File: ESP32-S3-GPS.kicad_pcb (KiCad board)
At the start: 2 copper layers, 75.6 x 87 mm, 46 parts, among them J1 PJ-102, J10 Conn_01x04_Pin, J11 Conn_01x04, J12 Conn_01x04, J2 Conn_01x03, J3 Conn_01x04, J4 Conn_01x05, J5 USB_B_Mini, J6 Conn_01x03_Pin, J7 Conn_01x02_Pin, J8 Conn_01x02_Pin, J9 Conn_02x04_Odd_Even, U1 AMS1117-5.0, U2 CH340N, U3 AMS1117-3.3, U5 ESP32-S3-DEVKITC-1-N8R2, U6 NRF24L01_Breakout

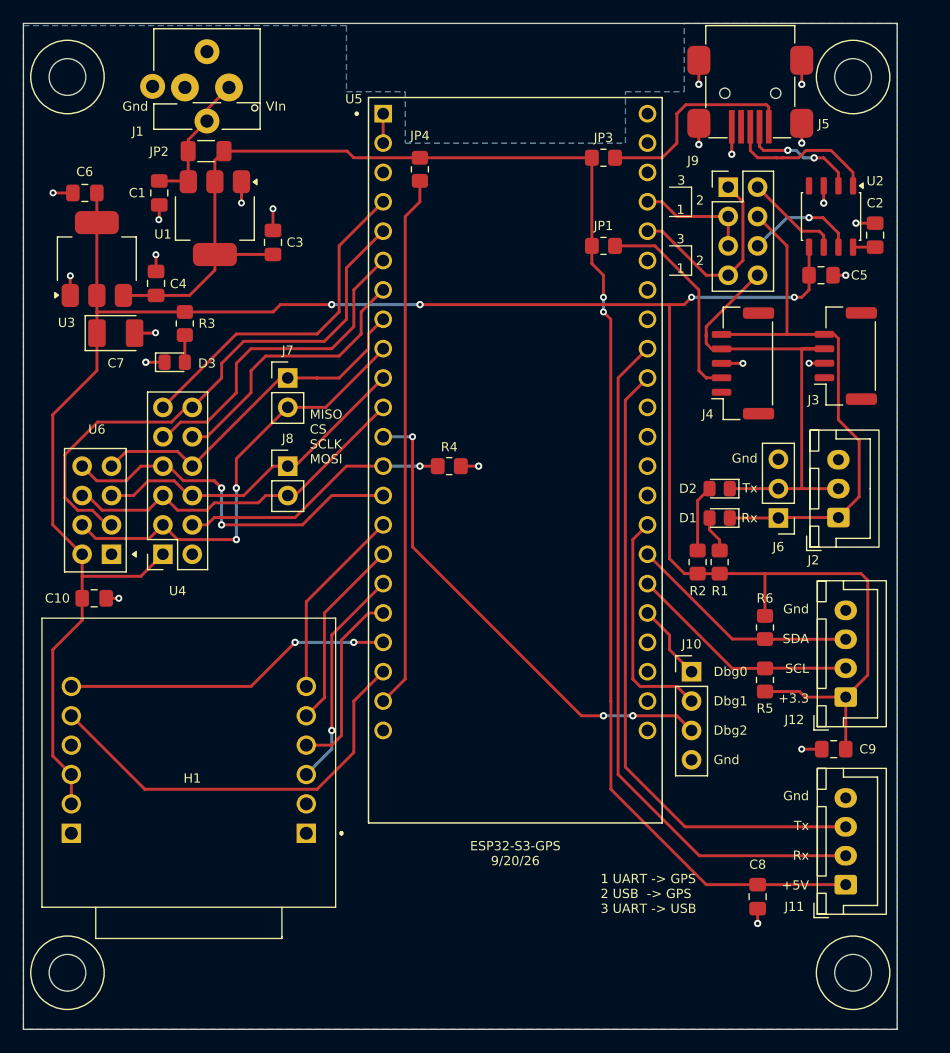
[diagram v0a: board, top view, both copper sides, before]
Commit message: Fix footprint for ESP32 DevKit Board.
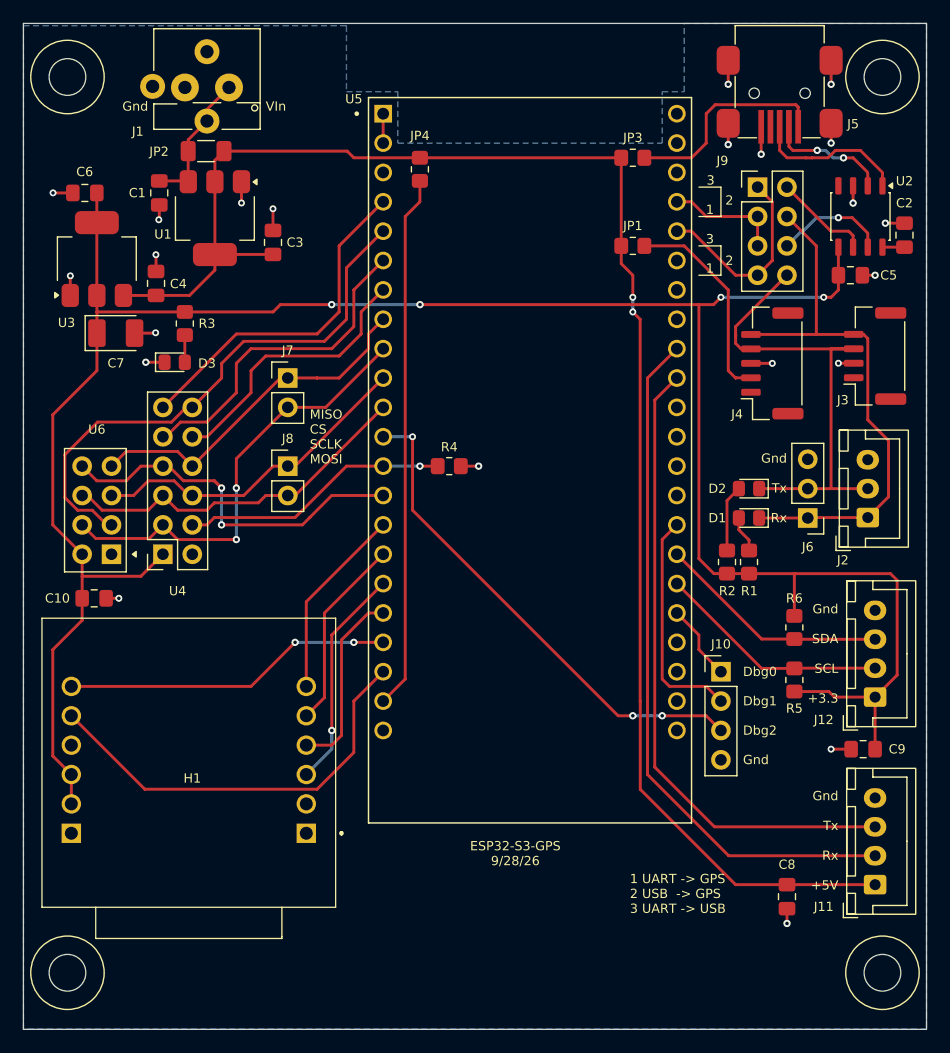
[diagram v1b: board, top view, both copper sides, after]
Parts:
- moved C5 2.54 mm to (188.4, 85.7)
- moved J2 2.54 mm to (189.9, 106.7)
- moved J4 2.54 mm to (181.6, 93.3)
- moved J6 2.54 mm to (184.7, 106.7)
- moved J9 2.54 mm to (180.3, 78.1)
- moved C2 2.54 mm to (193.0, 82.3)
- moved C8 2.54 mm to (182.9, 139.5)
- moved C9 2.54 mm to (189.5, 126.7)
- moved D1 2.54 mm to (179.6, 106.7)
- moved D2 2.54 mm to (179.6, 104.2)
- moved H4 2.54 mm to (191.1, 146.1)
- moved H5 2.54 mm to (191.1, 68.6)
- moved J10 2.54 mm to (177.2, 120.0)
- moved J11 2.54 mm to (190.5, 138.4)
- moved J12 2.54 mm to (190.5, 122.2)
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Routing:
- net +5V: track 135.5 -> 138.1 mm
- net +3V3: track 197.1 -> 199.6 mm
- net /Dbg2: track 42.8 -> 43.5 mm
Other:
- board size 75.6 x 87 mm -> 78.1 x 87 mm
- board text added: "ESP32-S3-GPS 9/28/26"
- board text removed: "ESP32-S3-GPS 9/20/26"

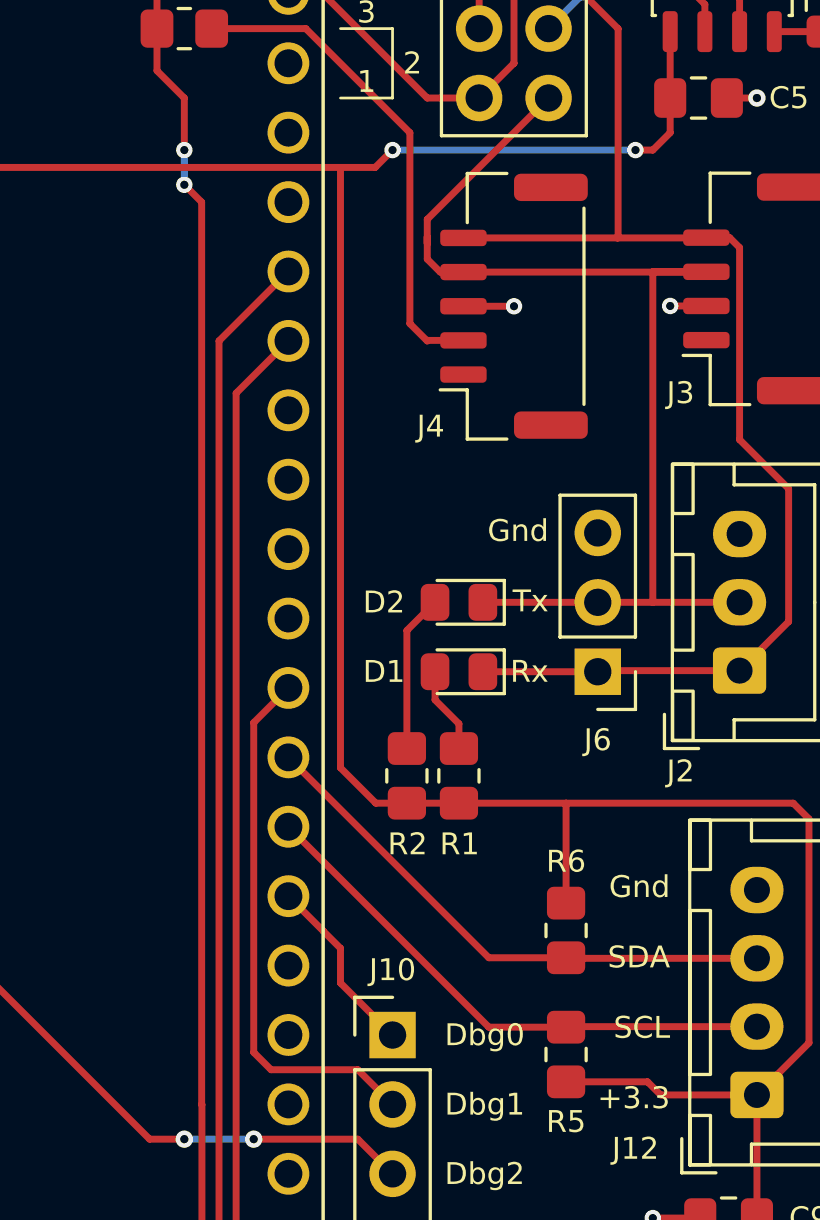
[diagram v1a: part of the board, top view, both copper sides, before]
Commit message: Change width of ESP32 Module footprint.  Change debug pin.
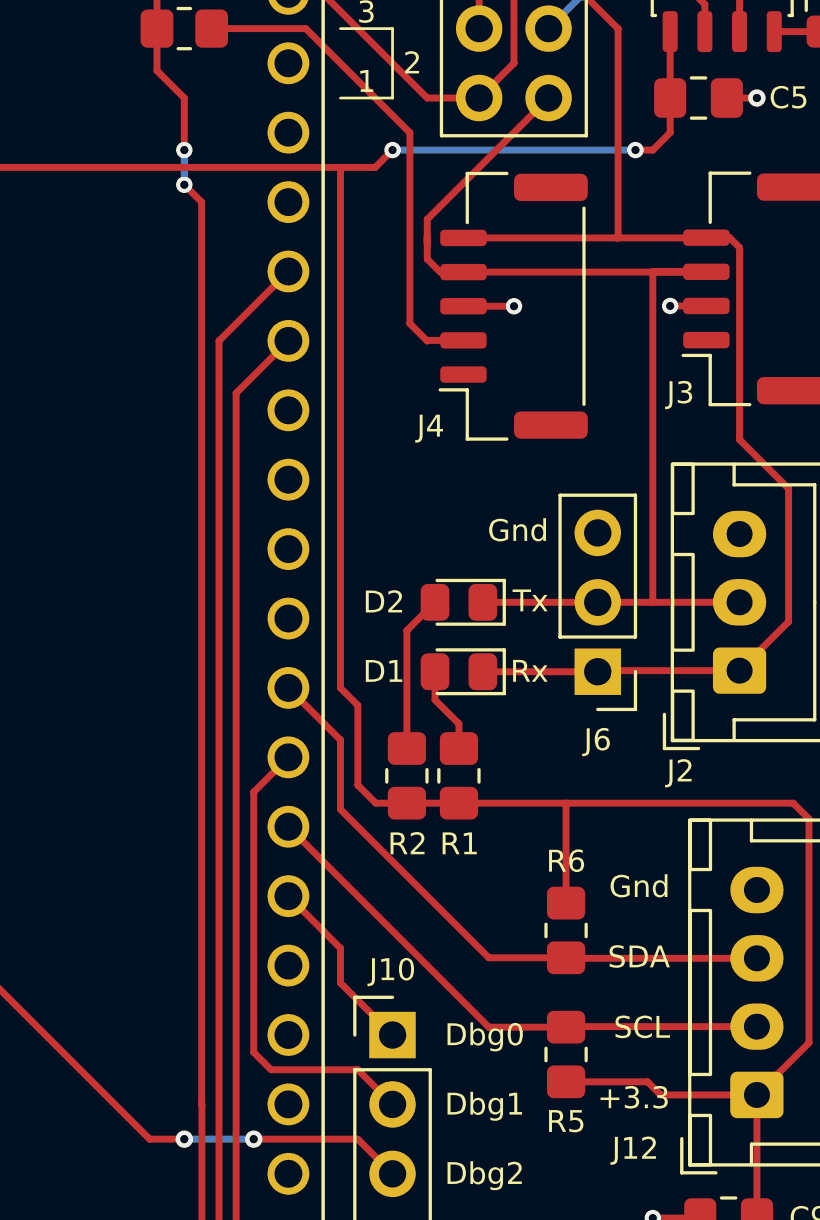
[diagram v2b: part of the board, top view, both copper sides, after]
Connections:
- U5 pad J3_15: /Dbg1 -> /SDA
- U5 pad J3_16: /SDA -> /Dbg1
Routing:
- net /SDA: track 20.2 -> 22.7 mm
- net /Dbg1: track 19.7 -> 17.2 mm
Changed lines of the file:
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@@
 		(sheetname "/")
 		(sheetfile "ESP32-S3-GPS.kicad_sch")
+		(units
+			(unit
+				(name "A")
+				(pins "J1_1" "J1_2" "J1_3" "J1_4" "J1_5" "J1_6" "J1_7" "J1_8" "J1_9"
+					"J1_10" "J1_11" "J1_12" "J1_13" "J1_14" "J1_15" "J1_16" "J1_17" "J1_18"
+					"J1_19" "J1_20" "J1_21" "J1_22" "J3_1" "J3_2" "J3_3" "J3_4" "J3_5" "J3_6"
+					"J3_7" "J3_8" "J3_9" "J3_10" "J3_11" "J3_12" "J3_13" "J3_14" "J3_15"
+					"J3_16" "J3_17" "J3_18" "J3_19" "J3_20" "J3_21" "J3_22"
+				)
+			)
+		)
 		(attr smd)
 		(duplicate_pad_numbers_are_jumpers no)
@@
 			(layers "*.Cu" "*.Mask")
 			(remove_unused_layers no)
-			(net "/Dbg1")
+			(net "/SDA")
 			(pinfunction "GPIO45_J3_15")
 			(pintype "bidirectional")
@@
 			(layers "*.Cu" "*.Mask")
 			(remove_unused_layers no)
-			(net "/SDA")
+			(net "/Dbg1")
 			(pinfunction "GPIO48_J3_16")
 			(pintype "bidirectional")
@@
 	)
 	(segment
+		(start 175.895 110.871)
+		(end 176.554 111.53)
+		(width 0.254)
+		(layer "F.Cu")
+		(net "+3V3")
+	)
+	(segment
 		(start 139.065 88.265)
 		(end 138.43 88.9)
@@
 	)
 	(segment
+		(start 175.26 107.315)
+		(end 175.895 107.95)
+		(width 0.254)
+		(layer "F.Cu")
+		(net "+3V3")
+	)
+	(segment
 		(start 192.405 120.3025)
 		(end 192.405 112.1075)
@@
 	)
 	(segment
+		(start 176.554 111.53)
+		(end 177.69 111.53)
+		(width 0.254)
+		(layer "F.Cu")
+		(net "+3V3")
+	)
+	(segment
 		(start 119.38 107.315)
 		(end 121.92 109.855)
@@
 	)
 	(segment
-		(start 176.554 111.53)
-		(end 177.69 111.53)
-		(width 0.254)
-		(layer "F.Cu")
-		(net "+3V3")
-	)
-	(segment
-		(start 175.26 88.265)
-		(end 175.26 110.236)
-		(width 0.254)
-		(layer "F.Cu")
-		(net "+3V3")
-	)
-	(segment
 		(start 121.92 113.665)
 		(end 121.92 111.76)
@@
 	)
 	(segment
+		(start 175.26 88.265)
+		(end 175.26 107.315)
+		(width 0.254)
+		(layer "F.Cu")
+		(net "+3V3")
+	)
+	(segment
 		(start 123.2 88.9)
 		(end 130.8 88.9)
@@
 	)
 	(segment
-		(start 175.26 110.236)
-		(end 176.554 111.53)
+		(start 187.325 85.725)
+		(end 187.325 86.995)
 		(width 0.254)
 		(layer "F.Cu")
@@
 	)
 	(segment
-		(start 187.325 85.725)
-		(end 187.325 86.995)
+		(start 175.895 107.95)
+		(end 175.895 110.871)
 		(width 0.254)
 		(layer "F.Cu")
@@
 	)
 	(segment
-		(start 172.085 108.583)
-		(end 173.355 107.313)
+		(start 172.72 121.285)
+		(end 172.085 120.65)
 		(width 0.254)
 		(layer "F.Cu")
@@
 	)
 	(segment
-		(start 172.72 121.285)
-		(end 172.085 120.65)
+		(start 172.085 120.65)
+		(end 172.085 111.123)
+		(width 0.254)
+		(layer "F.Cu")
+		(net "/Dbg1")
+	)
+	(segment
+		(start 172.085 111.123)
+		(end 173.355 109.853)
 		(width 0.254)
 		(layer "F.Cu")
@@
 	)
 	(segment
-		(start 172.085 120.65)
-		(end 172.085 108.583)
+		(start 175.26 111.76)
+		(end 175.26 109.218)
 		(width 0.254)
 		(layer "F.Cu")
-		(net "/Dbg1")
+		(net "/SDA")
 	)
 	(segment
@@
 	)
 	(segment
-		(start 183.515 117.1875)
-		(end 180.6895 117.1875)
+		(start 180.6875 117.1875)
+		(end 175.26 111.76)
 		(width 0.254)
 		(layer "F.Cu")
@@
 	)
 	(segment
-		(start 180.6895 117.1875)
-		(end 173.355 109.853)
+		(start 175.26 109.218)
+		(end 173.355 107.313)
+		(width 0.254)
+		(layer "F.Cu")
+		(net "/SDA")
+	)
+	(segment
+		(start 183.515 117.1875)
+		(end 180.6875 117.1875)
 		(width 0.254)
 		(layer "F.Cu")
